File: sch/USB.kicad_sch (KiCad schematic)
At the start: 18 parts, among them U4 CH340N, X1 GT-TF003-H0185-02

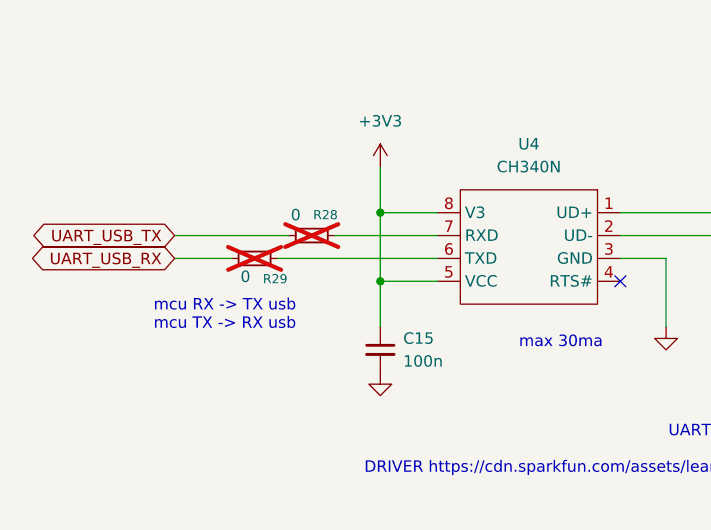
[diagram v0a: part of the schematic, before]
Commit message: v1.1 changes * increase LED resistors as they are too bright * replace solder jumpers with pins * add corresponding 3D models
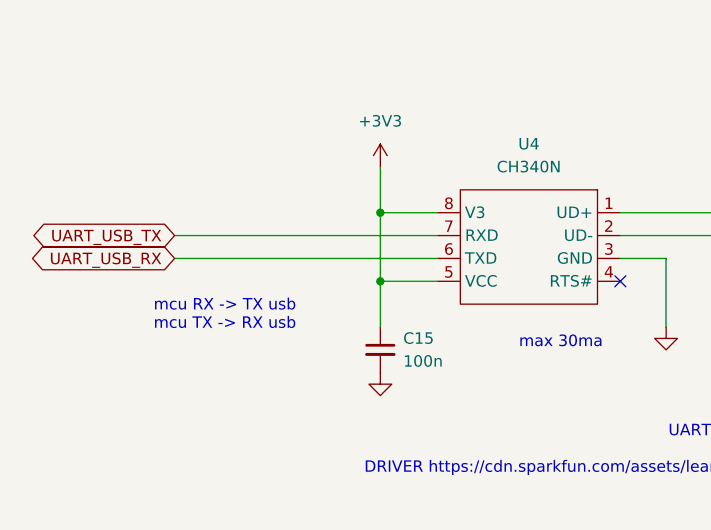
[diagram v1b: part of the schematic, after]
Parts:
- removed R28, R29: 0, EasyEDA_Lib:R0603, symbol Device:R_Small
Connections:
- net UART_USB_RX: now also U4.6 (TXD)
- net UART_USB_TX: now also U4.7 (RXD)
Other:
- title: 2CH CAN  Logger -> Dual Channel CAN Logger
